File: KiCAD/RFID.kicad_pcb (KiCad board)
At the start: 4 copper layers, 89.6 x 111.7 mm, 141 parts, among them IC1 TPS63020DSJR, IC2 BQ24075TRGTT, IC3 PN5321A3HN_C106,55, IC4 W25Q32JVSNIQ, J1 JST SH Con, J2 Conn_01x03_Pin, J3 Display Connector, J4 UJ20-C-H-G-MSMT-4B-P16-TR, J5 Battery Conenctor, J6 Conn_01x03_Pin, Q1 BSS84AK,215, Q3 NX7002AKVL, SW1 SW_Push, SW2 RUN, SW3 BOOTSEL, SW4 A_BTN, SW5 B_BTN, U1 RP2040, U2 BQ27441DRZR-G1A, Y1 27M12, Y2 12M

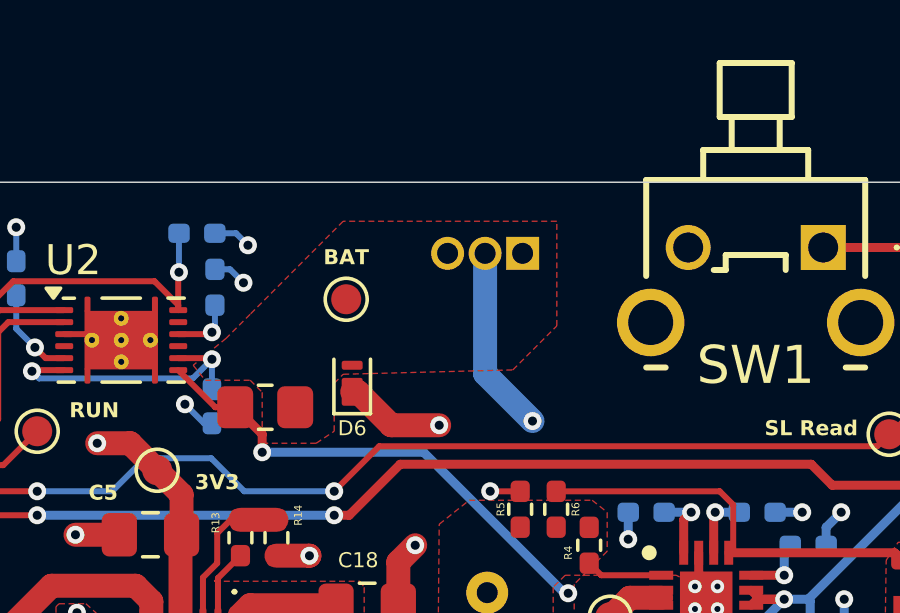
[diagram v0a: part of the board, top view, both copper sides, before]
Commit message: Corrected wrong battery footprint orientation
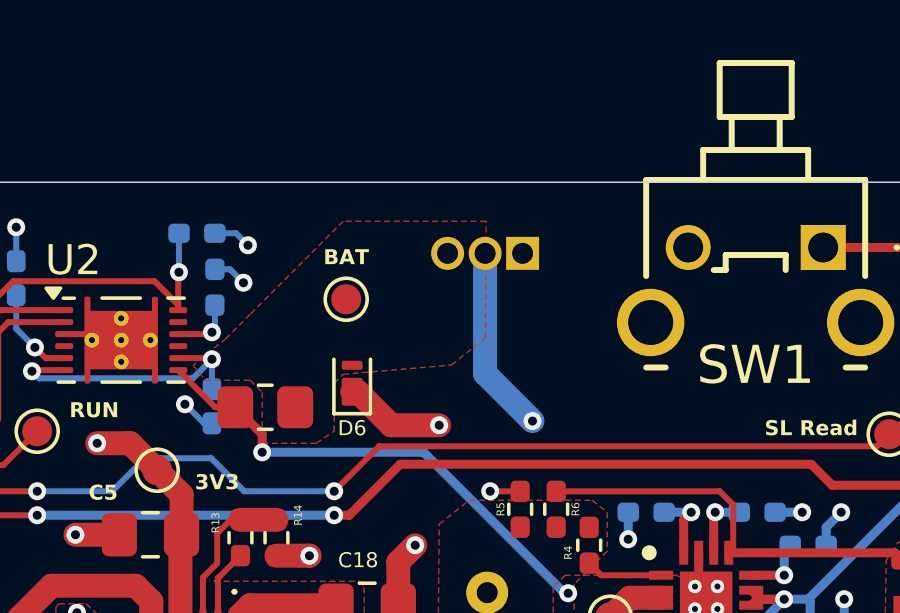
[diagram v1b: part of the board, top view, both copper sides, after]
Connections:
- J5 pad 1: /Battery Gauge/BAT -> unconnected-(J5-Pin_1-Pad1)
- J5 pad 3: unconnected-(J5-Pin_3-Pad3) -> /Battery Gauge/BAT
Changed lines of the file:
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@@
 			(layers "*.Cu" "*.Mask")
 			(remove_unused_layers no)
-			(net "/Battery Gauge/BAT")
+			(net "unconnected-(J5-Pin_1-Pad1)")
 			(pinfunction "Pin_1_1")
-			(pintype "passive")
+			(pintype "passive+no_connect")
 		)
 		(pad "2" thru_hole circle
@@
 			(layers "*.Cu" "*.Mask")
 			(remove_unused_layers no)
-			(net "unconnected-(J5-Pin_3-Pad3)")
+			(net "/Battery Gauge/BAT")
 			(pinfunction "Pin_3_3")
-			(pintype "passive+no_connect")
+			(pintype "passive")
 		)
 		(embedded_fonts no)
@@
 		(polygon
 			(pts
-				(xy 139.62 50.2) (xy 132.5 50.2) (xy 129.4 53.3) (xy 128.6 54.1) (xy 127.5 55) (xy 127.9 55.5) (xy 129.4 55.5)
-				(xy 129.8 55.9) (xy 129.8 57.6) (xy 131.6 57.6) (xy 132.2 57.2) (xy 132.2 55.6) (xy 132.5 55.3)
-				(xy 138.155 55.155) (xy 139.62 53.69)
+				(xy 137.265937 50.2) (xy 132.5 50.2) (xy 129.4 53.3) (xy 128.6 54.1) (xy 127.5 55) (xy 127.9 55.5)
+				(xy 129.4 55.5) (xy 129.8 55.9) (xy 129.8 57.6) (xy 131.6 57.6) (xy 132.2 57.2) (xy 132.2 55.6)
+				(xy 132.5 55.3) (xy 136.110614 54.992847) (xy 137.240637 54.086149)
 			)
 		)

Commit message: Added everything for ordering
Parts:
- C18, C45: footprint Capacitor_SMD:C_0805_2012Metric_Pad1.18x1.45mm_HandSolder -> Capacitor_SMD:C_0402_1005Metric_Pad0.74x0.62mm_HandSolder
- R1: value 46k8 -> 46k4
- moved C45 0.62 mm to (132.2, 66.8)
- moved C18 0.37 mm to (133.2, 62.6)
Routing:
- net /Buck-Boost/IN: track 88.1 -> 88.9 mm
- net GND: track 152.9 -> 152.4 mm
